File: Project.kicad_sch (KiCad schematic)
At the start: 75 parts, among them J1 Screw_Terminal_01x02, J2 Screw_Terminal_01x02, J3 Conn_01x04_Socket, Q1 BT136-500, SW1 PEC11H, SW2 PEC11H, U1 AMS1117-3.3, U2 ESP32-WROOM-32, U3 MOC3021M, U4 MCT2E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

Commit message: Added footprints
To-do finish list:
*Add connection LED disp<->MCU
*Assign footprints to:
Capacitors: 10,12,13,14,16,18,19,20;
Jumper JP1;
Mikrophone MK1;
*Assign 3d models;
*PCB design.
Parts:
- C11, C15: footprint (none) -> Capacitor_47uF:CAP_EEFK_D_PAN
- C17, C21: footprint (none) -> Capacitor_22uF:PCAP_125x25_PAN
- C6: footprint (none) -> Capacitor_100p:564R60GAT10_VIS
- C7: footprint (none) -> Capacitor_1uF:CAP_BFC237012105_VIS
- C8: footprint (none) -> Capacitor_0_01uF:CAP_BFC237035223_VIS
- C9: footprint (none) -> Capacitor_0_1uF:CAP_BFC233814104_VIS
- R10, R11, R12, R15, R21, R28, R9: footprint (none) -> Resistor_10k:RES_CFR25_TYCO_TYC
- R13, R16, R32: footprint (none) -> Resistor_2k:RES_TYCO_YR1_TYC
- R14: footprint (none) -> Resistor_100k:RES0402_CRG_TYCO_TYC
- R17, R19, R25, R27, R29, R31, RV1, RV2: footprint (none) -> Resistor_1M:RES0805_CRG_TYCO_TYC
- R20, R24, R30: footprint (none) -> Resistor_18k:RES0603_CRG_TYCO_TYC
- R22: footprint (none) -> Resistor_1k:RES_CFR200_TYCO_TYC
- R23: footprint (none) -> Resistor_47k:RES_CFR50_TYCO_TYC
- R26: footprint (none) -> Photoresistor:LDR1_NTE
- R33: footprint (none) -> Resistor_6_8k:RES_ROX1S_TYCO_TYC
- R34: footprint (none) -> Resistor_470k:RES0805_CRG_TYCO_TYC
- SW1, SW2: footprint (none) -> PEC11H_RE:PEC11H4025FS0016

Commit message: models
several 3d models were added
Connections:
- net GND: now also DS1.1 (VSS), DS1.20 (VSS)
- net VDD5: now also DS1.2 (VDD)
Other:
- note removed: "To connect LED to MCU"
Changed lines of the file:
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@@
+    (stroke (width 0) (type default))
+  )
+  (wire (pts (xy 71.12 92.71) (xy 74.93 92.71))
     (stroke (width 0) (type default))
   )
@@
   )
   (text "Power Transformer" (at 16.51 21.59 0)
-    (effects (font (size 1.27 1.27)) (justify left bottom))
-  )
-  (text "To connect LED to MCU" (at 55.88 97.79 0)
     (effects (font (size 1.27 1.27)) (justify left bottom))
   )
@@
     (property "Intersheetrefs" "${INTERSHEET_REFS}" (at 135.9287 147.32 0)
       (effects (font (size 1.27 1.27)) (justify right) hide)
+    )
+  )
+  (global_label "VDD5" (shape output) (at 71.12 62.23 0) (fields_autoplaced)
+    (effects (font (size 1.27 1.27)) (justify left))
+    (property "Intersheetrefs" "${INTERSHEET_REFS}" (at 78.8639 62.23 0)
+      (effects (font (size 1.27 1.27)) (justify left) hide)
     )
   )
@@
         )
       )
+    )
+  )
+  (symbol (lib_id "power:GND") (at 74.93 92.71 0) (unit 1)
+    (in_bom yes) (on_board yes) (dnp no) (fields_autoplaced)
+    (property "Reference" "#PWR019" (at 74.93 99.06 0)
+      (effects (font (size 1.27 1.27)) hide)
+    )
+    (property "Value" "GND" (at 74.93 97.79 0)
+      (effects (font (size 1.27 1.27)))
+    )
+    (property "Footprint" "" (at 74.93 92.71 0)
+      (effects (font (size 1.27 1.27)) hide)
+    )
+    (property "Datasheet" "" (at 74.93 92.71 0)
+      (effects (font (size 1.27 1.27)) hide)
+    )
+    (pin "1")
+    (instances
+      (project "Project"
+        (path "/90f0ab74-59db-459e-b705-994ce4b61f4e"
+          (reference "#PWR019") (unit 1)
+        )
+      )

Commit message: capacitors
capacitors footprints and resistor 3d models were added successfully
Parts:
- C10, C12, C13, C16, C19: footprint (none) -> Capacitor_10nF:CAPC1005X55N
- C14: footprint (none) -> Capacitor_5nF:CAP_1812_AVX
- C18, C20: footprint (none) -> Capacitor_100nF:WMF_08.1DX23.8LX0.6d_CND
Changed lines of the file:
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@@
       (effects (font (size 1.27 1.27)) (justify left))
     )
-    (property "Footprint" "" (at 106.3752 248.92 0)
+    (property "Footprint" "Capacitor_10nF:CAPC1005X55N" (at 106.3752 248.92 0)
       (effects (font (size 1.27 1.27)) hide)
     )
@@
       (effects (font (size 1.27 1.27)) (justify left))
     )
-    (property "Footprint" "" (at 188.9252 247.65 0)
+    (property "Footprint" "Capacitor_10nF:CAPC1005X55N" (at 188.9252 247.65 0)
       (effects (font (size 1.27 1.27)) hide)
     )
@@
       (effects (font (size 1.27 1.27)) (justify left))
     )
-    (property "Footprint" "" (at 41.6052 223.52 0)
+    (property "Footprint" "Capacitor_10nF:CAPC1005X55N" (at 41.6052 223.52 0)
       (effects (font (size 1.27 1.27)) hide)
     )
@@
       (effects (font (size 1.27 1.27)) (justify left))
     )
-    (property "Footprint" "" (at 91.1352 196.85 0)
+    (property "Footprint" "Capacitor_10nF:CAPC1005X55N" (at 91.1352 196.85 0)
       (effects (font (size 1.27 1.27)) hide)
     )
@@
       (effects (font (size 1.27 1.27)) (justify left))
     )
-    (property "Footprint" "" (at 106.3752 237.49 0)
+    (property "Footprint" "Capacitor_5nF:CAP_1812_AVX" (at 106.3752 237.49 0)
       (effects (font (size 1.27 1.27)) hide)
     )
@@
       (effects (font (size 1.27 1.27)) (justify left))
     )
-    (property "Footprint" "" (at 168.6052 247.65 0)
+    (property "Footprint" "Capacitor_100nF:WMF_08.1DX23.8LX0.6d_CND" (at 168.6052 247.65 0)
       (effects (font (size 1.27 1.27)) hide)
     )
@@
       (effects (font (size 1.27 1.27)) (justify left))
     )
-    (property "Footprint" "" (at 111.76 188.2648 0)
+    (property "Footprint" "Capacitor_100nF:WMF_08.1DX23.8LX0.6d_CND" (at 111.76 188.2648 0)
       (effects (font (size 1.27 1.27)) hide)
     )
@@
       (effects (font (size 1.27 1.27)) (justify left))
     )
-    (property "Footprint" "" (at 128.27 190.1952 0)
-      (effects (font (size 1.27 1.27)) hide)
-    )
+    (property "Footprint" "Capacitor_10nF:CAPC1005X55N" (at 128.27 190.1952 0)
+      (effects (font (size 1.27 1.27)) hide)
+    )

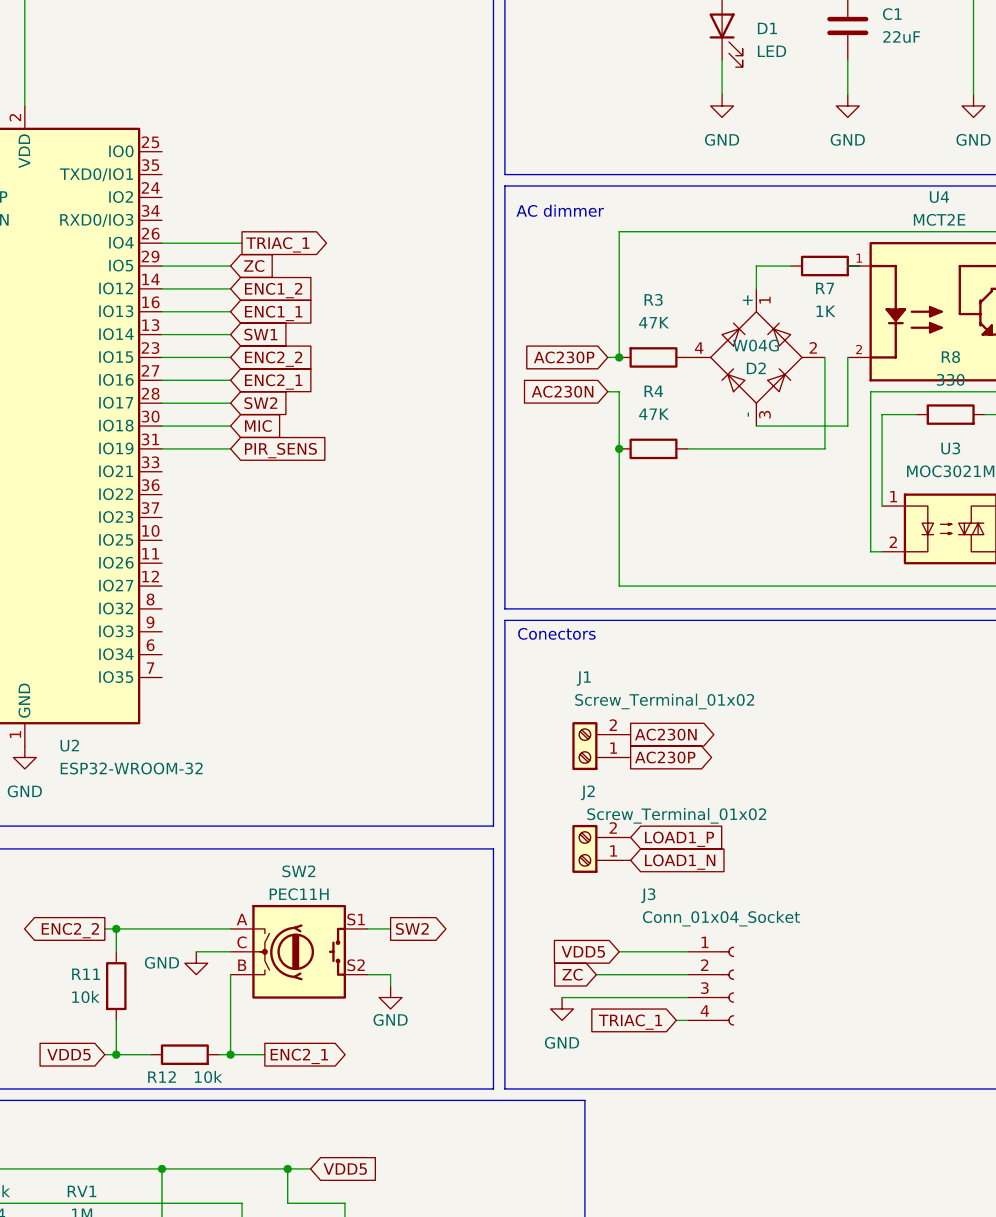
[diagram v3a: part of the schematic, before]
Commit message: UART and PCB Design rules
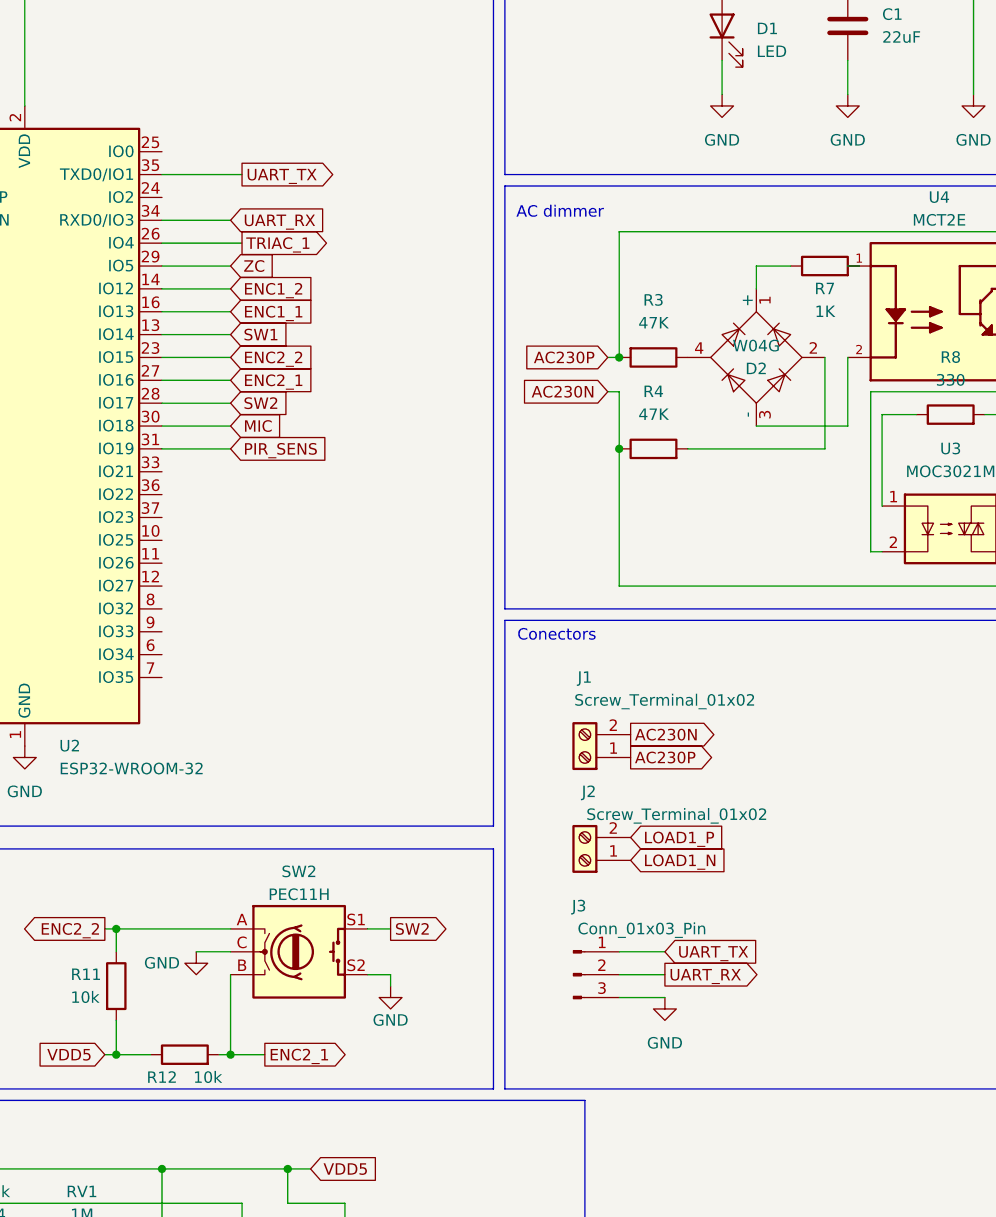
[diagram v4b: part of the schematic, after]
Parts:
- removed J3: Conn_01x04_Socket, Connector_PinHeader_1.27mm:PinHeader_1x04_P1.27mm_Vertical, symbol Connector:Conn_01x04_Socket
- added J3: Conn_01x03_Pin, Connector_PinHeader_1.00mm:PinHeader_1x03_P1.00mm_Horizontal, symbol Connector:Conn_01x03_Pin
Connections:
- net GND: now also J3.3 (Pin_3)
- net UART_RX: now reaches U2.34 (RXD0/IO3)
- net UART_RX: now also J3.2 (Pin_2)
- net UART_TX: now reaches U2.35 (TXD0/IO1)
- net UART_TX: now also J3.1 (Pin_1)
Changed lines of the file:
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@@
     (stroke (width 0) (type default))
   )
-  (wire (pts (xy 196.85 154.94) (xy 210.82 154.94))
-    (stroke (width 0) (type default))
-  )
   (wire (pts (xy 105.41 237.49) (xy 105.41 241.3))
     (stroke (width 0) (type default))
@@
     (stroke (width 0) (type default))
   )
-  (wire (pts (xy 203.2 149.86) (xy 210.82 149.86))
-    (stroke (width 0) (type default))
-  )
   (wire (pts (xy 147.32 147.32) (xy 147.32 149.86))
     (stroke (width 0) (type default))
@@
     (stroke (width 0) (type default))
   )
+  (wire (pts (xy 203.2 152.4) (xy 208.28 152.4))
+    (stroke (width 0) (type default))
+  )
   (wire (pts (xy 115.57 240.03) (xy 115.57 252.73))
     (stroke (width 0) (type default))
@@
     (stroke (width 0) (type default))
   )
-  (wire (pts (xy 200.66 152.4) (xy 210.82 152.4))
-    (stroke (width 0) (type default))
-  )
   (wire (pts (xy 50.8 140.97) (xy 57.15 140.97))
     (stroke (width 0) (type default))
@@
     (stroke (width 0) (type default))
   )
-  (wire (pts (xy 209.55 157.48) (xy 210.82 157.48))
+  (wire (pts (xy 152.4 68.58) (xy 160.02 68.58))
     (stroke (width 0) (type default))
   )
@@
     (stroke (width 0) (type default))
   )
+  (wire (pts (xy 203.2 154.94) (xy 208.28 154.94))
+    (stroke (width 0) (type default))
+  )
   (wire (pts (xy 30.48 252.73) (xy 30.48 213.36))
     (stroke (width 0) (type default))
@@
     (stroke (width 0) (type default))
   )
+  (wire (pts (xy 152.4 63.5) (xy 161.29 63.5))
+    (stroke (width 0) (type default))
+  )
   (wire (pts (xy 114.3 181.61) (xy 114.3 189.23))
     (stroke (width 0) (type default))
@@
     (stroke (width 0) (type default))
   )
+  (wire (pts (xy 203.2 149.86) (xy 208.28 149.86))
+    (stroke (width 0) (type default))
+  )
   (wire (pts (xy 275.59 97.79) (xy 275.59 69.85))
     (stroke (width 0) (type default))
@@
     (effects (font (size 1.27 1.27)) (justify left bottom))
   )
-  (global_label "VDD5" (shape input) (at 203.2 149.86 180) (fields_autoplaced)
-    (effects (font (size 1.27 1.27)) (justify right))
-    (property "Intersheetrefs" "${INTERSHEET_REFS}" (at 195.4561 149.86 0)
-      (effects (font (size 1.27 1.27)) (justify right) hide)
-    )
-  )
   (global_label "ZC" (shape output) (at 264.16 78.74 0) (fields_autoplaced)
     (effects (font (size 1.27 1.27)) (justify left))
@@
     )
   )
-  (global_label "ZC" (shape input) (at 200.66 152.4 180) (fields_autoplaced)
-    (effects (font (size 1.27 1.27)) (justify right))
-    (property "Intersheetrefs" "${INTERSHEET_REFS}" (at 195.2747 152.4 0)
-      (effects (font (size 1.27 1.27)) (justify right) hide)
-    )
-  )
-  (global_label "TRIAC_1" (shape input) (at 209.55 157.48 180) (fields_autoplaced)
-    (effects (font (size 1.27 1.27)) (justify right))
-    (property "Intersheetrefs" "${INTERSHEET_REFS}" (at 199.2661 157.48 0)
-      (effects (font (size 1.27 1.27)) (justify right) hide)
-    )
-  )
   (global_label "MIC" (shape output) (at 76.2 120.65 90) (fields_autoplaced)
     (effects (font (size 1.27 1.27)) (justify left))
@@
     )
   )
+  (global_label "UART_TX" (shape output) (at 161.29 63.5 0) (fields_autoplaced)
+    (effects (font (size 1.27 1.27)) (justify left))
+    (property "Intersheetrefs" "${INTERSHEET_REFS}" (at 171.9972 63.5 0)
+      (effects (font (size 1.27 1.27)) (justify left) hide)
+    )
+  )
   (global_label "AC230N" (shape input) (at 201.93 87.63 180) (fields_autoplaced)
     (effects (font (size 1.27 1.27)) (justify right))
@@
     )
   )
+  (global_label "UART_TX" (shape input) (at 208.28 149.86 0) (fields_autoplaced)
+    (effects (font (size 1.27 1.27)) (justify left))
+    (property "Intersheetrefs" "${INTERSHEET_REFS}" (at 218.9872 149.86 0)
+      (effects (font (size 1.27 1.27)) (justify left) hide)
+    )
+  )
   (global_label "PIR_SENS" (shape output) (at 165.1 214.63 0) (fields_autoplaced)
     (effects (font (size 1.27 1.27)) (justify left))
@@
     )
   )
+  (global_label "UART_RX" (shape input) (at 160.02 68.58 0) (fields_autoplaced)
+    (effects (font (size 1.27 1.27)) (justify left))
+    (property "Intersheetrefs" "${INTERSHEET_REFS}" (at 171.0296 68.58 0)
+      (effects (font (size 1.27 1.27)) (justify left) hide)
+    )
+  )
+  (global_label "UART_RX" (shape output) (at 208.28 152.4 0) (fields_autoplaced)
+    (effects (font (size 1.27 1.27)) (justify left))
+    (property "Intersheetrefs" "${INTERSHEET_REFS}" (at 219.2896 152.4 0)
+      (effects (font (size 1.27 1.27)) (justify left) hide)
+    )
+  )
   (global_label "TRIAC_1" (shape input) (at 264.16 83.82 0) (fields_autoplaced)
     (effects (font (size 1.27 1.27)) (justify left))
@@
     )
   )
+  (symbol (lib_id "power:GND") (at 208.28 154.94 0) (unit 1)
+    (in_bom yes) (on_board yes) (dnp no) (fields_autoplaced)
+    (property "Reference" "#PWR09" (at 208.28 161.29 0)
+      (effects (font (size 1.27 1.27)) hide)
+    )
+    (property "Value" "GND" (at 208.28 160.02 0)
+      (effects (font (size 1.27 1.27)))
+    )
+    (property "Footprint" "" (at 208.28 154.94 0)
+      (effects (font (size 1.27 1.27)) hide)
+    )
+    (property "Datasheet" "" (at 208.28 154.94 0)
+      (effects (font (size 1.27 1.27)) hide)
+    )
+    (pin "1")
+    (instances
+      (project "Project"
+        (path "/90f0ab74-59db-459e-b705-994ce4b61f4e"
+          (reference "#PWR09") (unit 1)
+        )
+      )
+    )
+  )
   (symbol (lib_id "Device:R") (at 115.57 236.22 180) (unit 1)
     (in_bom yes) (on_board yes) (dnp no)
@@
     )
   )
-  (symbol (lib_id "power:GND") (at 196.85 154.94 0) (unit 1)
-    (in_bom yes) (on_board yes) (dnp no) (fields_autoplaced)
-    (property "Reference" "#PWR09" (at 196.85 161.29 0)
+  (symbol (lib_id "power:GND") (at 25.4 154.94 0) (unit 1)
+    (in_bom yes) (on_board yes) (dnp no)
+    (property "Reference" "#PWR016" (at 25.4 161.29 0)
       (effects (font (size 1.27 1.27)) hide)
     )
-    (property "Value" "GND" (at 196.85 160.02 0)
+    (property "Value" "GND" (at 25.4 158.75 0)
       (effects (font (size 1.27 1.27)))
     )
-    (property "Footprint" "" (at 196.85 154.94 0)
+    (property "Footprint" "" (at 25.4 154.94 0)
       (effects (font (size 1.27 1.27)) hide)
     )
-    (property "Datasheet" "" (at 196.85 154.94 0)
+    (property "Datasheet" "" (at 25.4 154.94 0)
       (effects (font (size 1.27 1.27)) hide)
     )
@@
       (project "Project"
         (path "/90f0ab74-59db-459e-b705-994ce4b61f4e"
-          (reference "#PWR09") (unit 1)
+          (reference "#PWR016") (unit 1)
         )
       )
     )
   )
-  (symbol (lib_id "power:GND") (at 25.4 154.94 0) (unit 1)
+  (symbol (lib_id "Connector:Conn_01x03_Pin") (at 198.12 152.4 0) (unit 1)
     (in_bom yes) (on_board yes) (dnp no)
-    (property "Reference" "#PWR016" (at 25.4 161.29 0)
-      (effects (font (size 1.27 1.27)) hide)
+    (property "Reference" "J3" (at 198.755 144.78 0)
+      (effects (font (size 1.27 1.27)))
     )
-    (property "Value" "GND" (at 25.4 158.75 0)
+    (property "Value" "Conn_01x03_Pin" (at 205.74 147.32 0)
       (effects (font (size 1.27 1.27)))
     )
-    (property "Footprint" "" (at 25.4 154.94 0)
+    (property "Footprint" "Connector_PinHeader_1.00mm:PinHeader_1x03_P1.00mm_Horizontal" (at 198.12 152.4 0)
       (effects (font (size 1.27 1.27)) hide)
     )
-    (property "Datasheet" "" (at 25.4 154.94 0)
+    (property "Datasheet" "~" (at 198.12 152.4 0)
       (effects (font (size 1.27 1.27)) hide)
     )
     (pin "1")
+    (pin "2")
+    (pin "3")
     (instances
       (project "Project"
         (path "/90f0ab74-59db-459e-b705-994ce4b61f4e"
-          (reference "#PWR016") (unit 1)
+          (reference "J3") (unit 1)
         )
       )
@@
         )
       )
-    )
-  )
-  (symbol (lib_id "Connector:Conn_01x04_Socket") (at 215.9 152.4 0) (unit 1)
-    (in_bom yes) (on_board yes) (dnp no)
-    (property "Reference" "J3" (at 205.74 143.51 0)
-      (effects (font (size 1.27 1.27)) (justify left))
-    )
-    (property "Value" "Conn_01x04_Socket" (at 205.74 146.05 0)
-      (effects (font (size 1.27 1.27)) (justify left))
-    )
-    (property "Footprint" "Connector_PinHeader_1.27mm:PinHeader_1x04_P1.27mm_Vertical" (at 215.9 152.4 0)
-      (effects (font (size 1.27 1.27)) hide)
-    )
-    (property "Datasheet" "~" (at 215.9 152.4 0)
-      (effects (font (size 1.27 1.27)) hide)
-    )
-    (pin "1")
-    (pin "2")
-    (pin "3")
-    (pin "4")
-    (instances
-      (project "Project"
-        (path "/90f0ab74-59db-459e-b705-994ce4b61f4e"
-          (reference "J3") (unit 1)
-        )
-      )
